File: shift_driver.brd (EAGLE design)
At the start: 100 x 90 mm, 28 parts, among them IC1 7805T, IC2 74HC595D, IC3 74HC595D, IC4 74HC595D, IC5 74HC595D, IC6 74HC595D, IC7 74HC595D

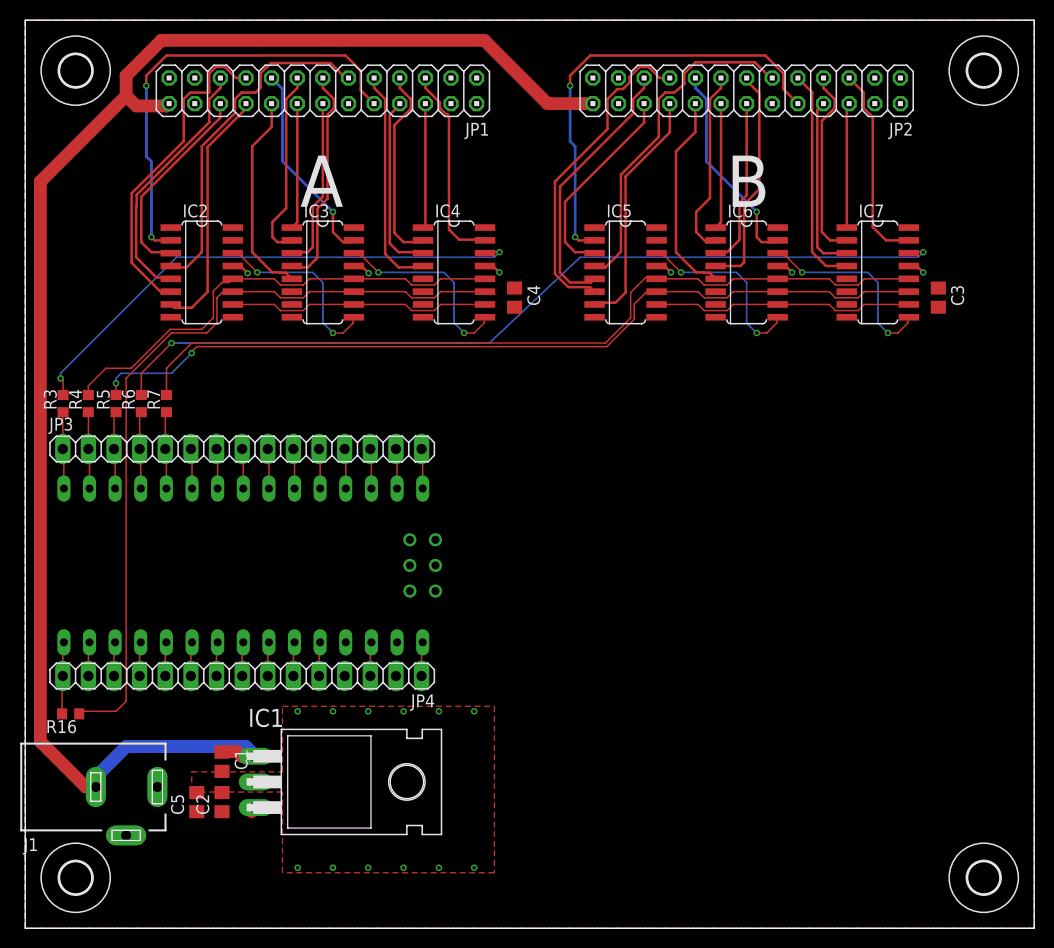
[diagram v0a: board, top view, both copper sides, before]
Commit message: Routed remaining. Fixed DRC. Added proto area.
Added design rules from seeedstudio and fixed some weird problems with
DRC that came with it. Better clearance to everything now.
Added a prototyping area for future expansion.
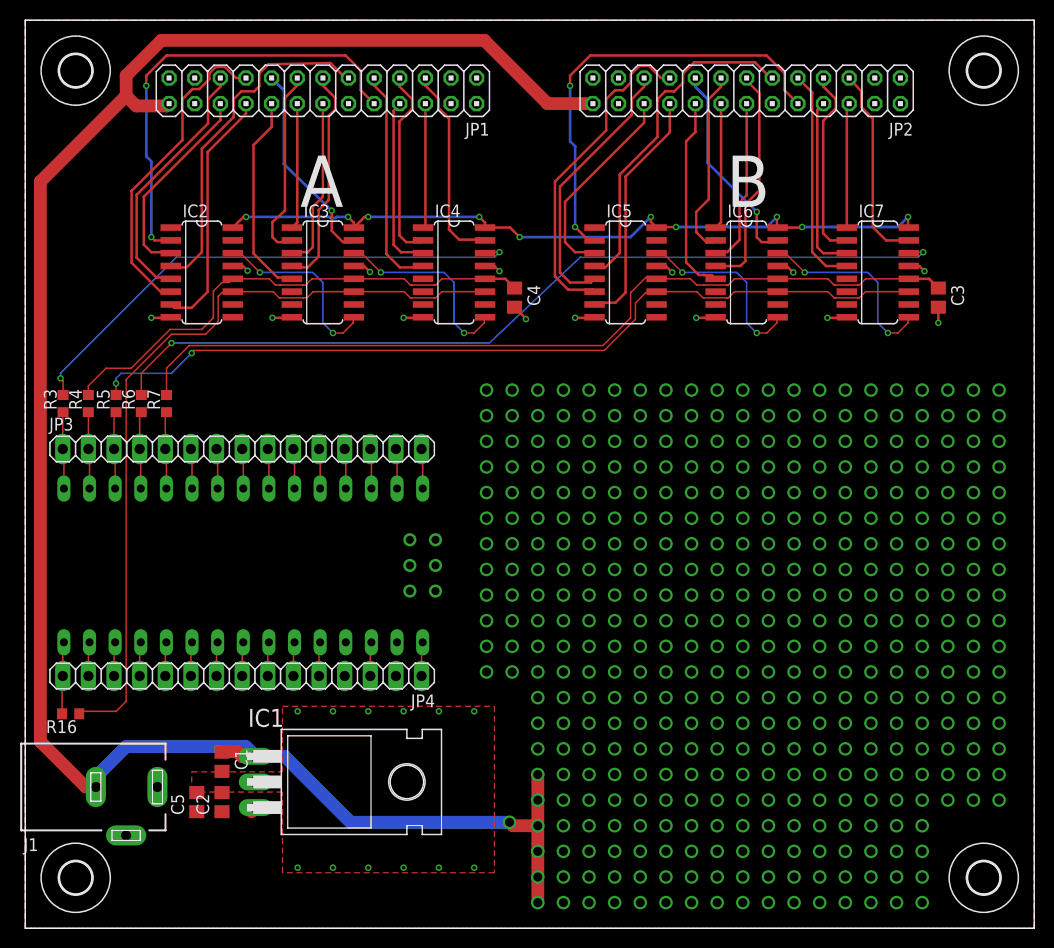
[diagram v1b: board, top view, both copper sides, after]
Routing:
- net VCC: track 0.00 -> 74.2 mm, vias 0 -> 10
- net +5V: track 52.6 -> 0.58 mm, vias 0 -> 7
- net +24V: track 154.0 -> 197.5 mm, vias 0 -> 7
- net GND: track 10.3 -> 25.4 mm, vias 18 -> 34
- net LATCH_B: track 82.5 -> 85.9 mm
- net LATCH_A: track 47.2 -> 50.5 mm
- net B18: track 20.5 -> 19.7 mm
- net A19: track 32.6 -> 32.0 mm
- net B10: track 44.6 -> 44.0 mm

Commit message: Route last wires, finishing touches and small fixes.
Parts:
- J1: device con-jack:DCJ0303 -> AH_components:DCJ0303
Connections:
- net +24V: now also J1.1; no longer J1.3
- net GND: now also J1.3; no longer J1.1
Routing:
- net +24V: track 197.5 -> 194.8 mm
- net A10: track 44.8 -> 45.4 mm
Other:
- board text added: "24V"
- board text added: "5V"
- board text added: "ADMITTANSEN Flipdot driver August Hultman Nils Hallkvist 2017"
- board text added: "Clock_A"
- board text added: "Clock_B"
- board text added: "Data_A"
- board text added: "Data_B"
- board text added: "GND"
- board text added: "Latch_A"
- board text added: "Latch_B"

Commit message: Add code and latest board file
Code for arduino and PC
Minor changes to board file
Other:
- board size 100 x 90 mm -> 99.5 x 90 mm
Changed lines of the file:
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@@
 <?xml version="1.0" encoding="utf-8"?>
 <!DOCTYPE eagle SYSTEM "eagle.dtd">
-<eagle version="8.3.2">
+<eagle version="8.4.2">
 <drawing>
 <settings>
@@
 <layer number="59" name="tCarbon" color="7" fill="1" visible="no" active="no"/>
 <layer number="60" name="bCarbon" color="7" fill="1" visible="no" active="no"/>
-<layer number="88" name="SimResults" color="9" fill="1" visible="no" active="yes"/>
-<layer number="89" name="SimProbes" color="9" fill="1" visible="no" active="yes"/>
+<layer number="88" name="SimResults" color="9" fill="1" visible="no" active="no"/>
+<layer number="89" name="SimProbes" color="9" fill="1" visible="no" active="no"/>
 <layer number="90" name="Modules" color="5" fill="1" visible="no" active="no"/>
 <layer number="91" name="Nets" color="2" fill="1" visible="no" active="no"/>
@@
 <board>
 <plain>
-<wire x1="0" y1="0" x2="100" y2="0" width="0" layer="20"/>
-<wire x1="100" y1="0" x2="100" y2="90" width="0" layer="20"/>
-<wire x1="100" y1="90" x2="0" y2="90" width="0" layer="20"/>
+<wire x1="0" y1="0" x2="99.5" y2="0" width="0" layer="20"/>
+<wire x1="99.5" y1="0" x2="99.5" y2="90" width="0" layer="20"/>
+<wire x1="99.5" y1="90" x2="0" y2="90" width="0" layer="20"/>
 <wire x1="0" y1="90" x2="0" y2="0" width="0" layer="20"/>
 <text x="27.25" y="71.5" size="5.08" layer="21">A</text>
 <text x="69.5" y="71.5" size="5.08" layer="21">B</text>
 <polygon width="0.254" layer="41">
-<vertex x="100" y="55"/>
+<vertex x="99.5" y="55"/>
 <vertex x="44" y="55"/>
 <vertex x="44" y="34.5"/>
@@
 <vertex x="48.5" y="16"/>
 <vertex x="48.5" y="0"/>
-<vertex x="100" y="0"/>
+<vertex x="99.5" y="0"/>
 </polygon>
 <polygon width="0.254" layer="42">
 <vertex x="47" y="55"/>
-<vertex x="100" y="55"/>
-<vertex x="100" y="0"/>
+<vertex x="99.5" y="55"/>
+<vertex x="99.5" y="0"/>
 <vertex x="47.25" y="0"/>
 <vertex x="47.25" y="24"/>
@@
 <param name="dpMaxLengthDifference" value="10mm"/>
 <param name="dpGapFactor" value="2.5"/>
-<param name="checkGrid" value="0"/>
 <param name="checkAngle" value="0"/>
 <param name="checkFont" value="1"/>
 <param name="checkRestrict" value="0"/>
+<param name="checkStop" value="0"/>
 <param name="useDiameter" value="13"/>
 <param name="maxErrors" value="50"/>
@@
 <vertex x="0" y="90"/>
 <vertex x="0" y="0"/>
-<vertex x="100" y="0"/>
-<vertex x="100" y="90"/>
+<vertex x="99.5" y="0"/>
+<vertex x="99.5" y="90"/>
 </polygon>
 <contactref element="C3" pad="2"/>
@@
 <vertex x="0" y="0"/>
 <vertex x="0" y="90"/>
-<vertex x="100" y="90"/>
-<vertex x="100" y="0"/>
+<vertex x="99.5" y="90"/>
+<vertex x="99.5" y="0"/>
 </polygon>
 <via x="27" y="21.5" extent="1-16" drill="0.35"/>
@@
 <polygon width="0.1524" layer="1" isolate="0.3" rank="3">
 <vertex x="0" y="90"/>
-<vertex x="100" y="90"/>
-<vertex x="100" y="0"/>
+<vertex x="99.5" y="90"/>
+<vertex x="99.5" y="0"/>
 <vertex x="0" y="0"/>
 </polygon>
